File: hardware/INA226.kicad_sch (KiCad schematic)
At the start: 6 parts, among them U501 INA226

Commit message: Tracing 2
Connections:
- net VIN+ renamed VIN
- net VIN- renamed VOUT
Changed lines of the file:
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@@
 		)
 	)
-	(hierarchical_label "VIN+"
+	(hierarchical_label "VIN"
 		(shape input)
 		(at 91.44 96.52 180)
@@
 		)
 	)
-	(hierarchical_label "VIN-"
+	(hierarchical_label "VOUT"
 		(shape input)
 		(at 91.44 109.22 180)

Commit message: Tracing 3
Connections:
- net ALERT: now reaches U501.3 (~{Alert})
- no-connect marks 1 -> 0
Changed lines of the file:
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@@
 		(color 0 0 0 0)
-	)
-	(no_connect
-		(at 156.21 101.6)
 	)
 	(wire
@@
 		(effects
 			(font
+				(size 1.27 1.27)
+			)
+			(justify left)
+		)
+	)
+	(hierarchical_label "ALERT"
+		(shape input)
+		(at 156.21 101.6 0)
+		(effects
+			(font

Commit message: Fixes
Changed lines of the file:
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@@
 	)
 	(hierarchical_label "ALERT"
-		(shape input)
+		(shape output)
 		(at 156.21 101.6 0)
 		(effects

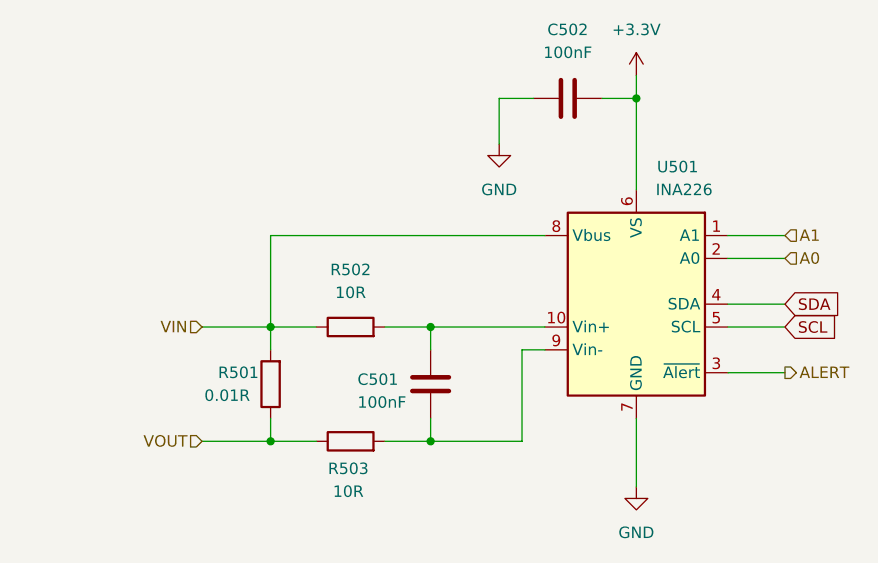
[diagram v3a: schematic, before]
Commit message: thermal relief
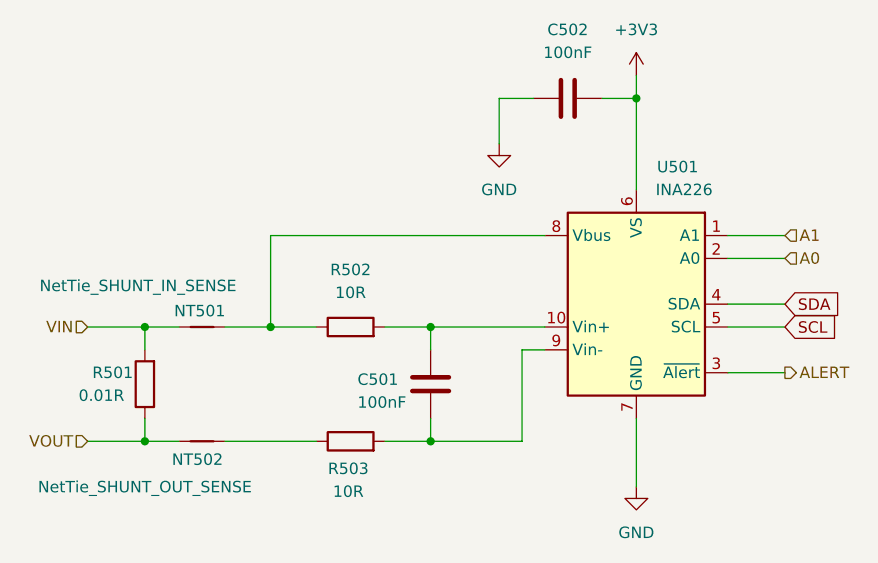
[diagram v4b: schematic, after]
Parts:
- added NT501: NetTie_SHUNT_IN_SENSE, NetTie:NetTie-2_SMD_Pad0.5mm, symbol Device:NetTie_2
- added NT502: NetTie_SHUNT_OUT_SENSE, NetTie:NetTie-2_SMD_Pad0.5mm, symbol Device:NetTie_2
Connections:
- net VIN: now also NT501.1; no longer R502.1, U501.8 (Vbus)
- net VOUT: now also NT502.1; no longer R503.1
- net +3.3V renamed +3V3
- new net: NT502.2, R503.1
- new net: NT501.2, R502.1, U501.8 (Vbus)
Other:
- moved on the sheet: R501
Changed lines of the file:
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@@
+	)
+	(junction
+		(at 85.09 109.22)
+		(diameter 0)
+		(color 0 0 0 0)
+	)
+	(junction
+		(at 85.09 96.52)
+		(diameter 0)
+		(color 0 0 0 0)
 	)
 	(junction
@@
 		(color 0 0 0 0)
 	)
-	(junction
-		(at 99.06 109.22)
-		(diameter 0)
-		(color 0 0 0 0)
-	)
-	(wire
-		(pts
-			(xy 91.44 96.52) (xy 99.06 96.52)
+	(wire
+		(pts
+			(xy 78.74 109.22) (xy 85.09 109.22)
 		)
 		(stroke
@@
 	(wire
 		(pts
-			(xy 91.44 109.22) (xy 99.06 109.22)
-		)
-		(stroke
-			(width 0)
-			(type default)
-		)
-	)
-	(wire
-		(pts
 			(xy 116.84 96.52) (xy 116.84 99.06)
 		)
@@
 	(wire
 		(pts
+			(xy 93.98 96.52) (xy 99.06 96.52)
+		)
+		(stroke
+			(width 0)
+			(type default)
+		)
+	)
+	(wire
+		(pts
 			(xy 99.06 86.36) (xy 129.54 86.36)
 		)
@@
 	(wire
 		(pts
-			(xy 104.14 109.22) (xy 99.06 109.22)
+			(xy 85.09 96.52) (xy 88.9 96.52)
+		)
+		(stroke
+			(width 0)
+			(type default)
+		)
+	)
+	(wire
+		(pts
+			(xy 93.98 109.22) (xy 104.14 109.22)
 		)
 		(stroke
@@
 	(wire
 		(pts
+			(xy 78.74 96.52) (xy 85.09 96.52)
+		)
+		(stroke
+			(width 0)
+			(type default)
+		)
+	)
+	(wire
+		(pts
 			(xy 124.46 71.12) (xy 124.46 76.2)
 		)
@@
 	(wire
 		(pts
-			(xy 99.06 96.52) (xy 99.06 99.06)
+			(xy 85.09 109.22) (xy 88.9 109.22)
 		)
 		(stroke
@@
 	(wire
 		(pts
+			(xy 85.09 109.22) (xy 85.09 106.68)
+		)
+		(stroke
+			(width 0)
+			(type default)
+		)
+	)
+	(wire
+		(pts
 			(xy 127 99.06) (xy 129.54 99.06)
 		)
@@
 	(wire
 		(pts
-			(xy 99.06 109.22) (xy 99.06 106.68)
+			(xy 85.09 96.52) (xy 85.09 99.06)
 		)
 		(stroke
@@
 	(hierarchical_label "VIN"
 		(shape input)
-		(at 91.44 96.52 180)
+		(at 78.74 96.52 180)
 		(effects
 			(font
@@
 	(hierarchical_label "VOUT"
 		(shape input)
-		(at 91.44 109.22 180)
+		(at 78.74 109.22 180)
 		(effects
 			(font
@@
 	(symbol
 		(lib_id "Device:R")
-		(at 99.06 102.87 180)
+		(at 85.09 102.87 180)
 		(unit 1)
 		(exclude_from_sim no)
@@
 		(dnp no)
 		(property "Reference" "R501"
-			(at 93.218 101.6 0)
+			(at 79.248 101.6 0)
 			(effects
 				(font
@@
 		)
 		(property "Value" "0.01R"
-			(at 91.694 104.14 0)
+			(at 77.724 104.14 0)
 			(effects
 				(font
@@
 		)
 		(property "Footprint" "Resistor_SMD:R_2512_6332Metric_Pad1.40x3.35mm_HandSolder"
-			(at 100.838 102.87 90)
+			(at 86.868 102.87 90)
 			(effects
 				(font
@@
 		)
 		(property "Datasheet" "~"
-			(at 99.06 102.87 0)
+			(at 85.09 102.87 0)
 			(effects
 				(font
@@
 		)
 		(property "Description" "Resistor"
-			(at 99.06 102.87 0)
+			(at 85.09 102.87 0)
 			(effects
 				(font
@@
 	)
 	(symbol
+		(lib_id "Device:NetTie_2")
+		(at 91.44 109.22 0)
+		(unit 1)
+		(exclude_from_sim no)
+		(in_bom no)
+		(on_board yes)
+		(dnp no)
+		(property "Reference" "NT502"
+			(at 90.932 111.252 0)
+			(effects
+				(font
+					(size 1.27 1.27)
+				)
+			)
+		)
+		(property "Value" "NetTie_SHUNT_OUT_SENSE"
+			(at 85.09 114.3 0)
+			(effects
+				(font
+					(size 1.27 1.27)
+				)
+			)
+		)
+		(property "Footprint" "NetTie:NetTie-2_SMD_Pad0.5mm"
+			(at 91.44 109.22 0)
+			(effects
+				(font
+					(size 1.27 1.27)
+				)
+				(hide yes)
+			)
+		)
+		(property "Datasheet" "~"
+			(at 91.44 109.22 0)
+			(effects
+				(font
+					(size 1.27 1.27)
+				)
+				(hide yes)
+			)
+		)
+		(property "Description" "Net tie, 2 pins"
+			(at 91.44 109.22 0)
+			(effects
+				(font
+					(size 1.27 1.27)
+				)
+				(hide yes)
+			)
+		)
+		(pin "2"
+		)
+		(pin "1"
+		)
+		(instances
+			(project ""
+				(path "/2a3ef4c2-927a-45cd-a4f2-5ee83a7e9444/4bc00da0-4814-43a9-a32d-b93b905ddfeb"
+					(reference "NT602")
+					(unit 1)
+				)
+				(path "/2a3ef4c2-927a-45cd-a4f2-5ee83a7e9444/f962763b-4c4d-46df-88bc-cd86339d95d6"
+					(reference "NT702")
+					(unit 1)
+				)
+				(path "/2a3ef4c2-927a-45cd-a4f2-5ee83a7e9444/56c5dda2-1e55-4d6c-a70d-c1acd647cefd/f8324967-96b4-4b60-9438-d68c8ddcfb61"
+					(reference "NT1202")
+					(unit 1)
+				)
+				(path "/2a3ef4c2-927a-45cd-a4f2-5ee83a7e9444/865d6fe0-7870-4134-be7f-c35221518457/f8324967-96b4-4b60-9438-d68c8ddcfb61"
+					(reference "NT502")
+					(unit 1)
+				)
+				(path "/2a3ef4c2-927a-45cd-a4f2-5ee83a7e9444/b3941ffe-e8e1-48f3-a016-360d76a87258/f8324967-96b4-4b60-9438-d68c8ddcfb61"
+					(reference "NT1002")
+					(unit 1)
+				)
+			)
+		)
+	)
+	(symbol
 		(lib_id "power:+3.3V")
 		(at 139.7 68.58 0)
@@
 			)
 		)
-		(property "Value" "+3.3V"
+		(property "Value" "+3V3"
 			(at 139.7 63.5 0)
 			(effects
@@
 					(unit 1)
 				)
+			)
+		)
+	)
+	(symbol
+		(lib_id "Device:NetTie_2")
+		(at 91.44 96.52 0)
+		(unit 1)
+		(exclude_from_sim no)
+		(in_bom no)
+		(on_board yes)
+		(dnp no)
+		(property "Reference" "NT501"
+			(at 91.186 94.742 0)
+			(effects
+				(font
+					(size 1.27 1.27)
+				)
+			)
+		)
+		(property "Value" "NetTie_SHUNT_IN_SENSE"
+			(at 84.328 91.948 0)
+			(effects
+				(font
+					(size 1.27 1.27)
+				)
+			)
+		)
+		(property "Footprint" "NetTie:NetTie-2_SMD_Pad0.5mm"
+			(at 91.44 96.52 0)
+			(effects
+				(font
+					(size 1.27 1.27)
+				)
+				(hide yes)
+			)
+		)
+		(property "Datasheet" "~"
+			(at 91.44 96.52 0)
+			(effects
+				(font
+					(size 1.27 1.27)
+				)
+				(hide yes)
+			)
+		)
+		(property "Description" "Net tie, 2 pins"
+			(at 91.44 96.52 0)
+			(effects
+				(font
+					(size 1.27 1.27)
+				)
+				(hide yes)
+			)
+		)
+		(pin "1"
+		)
+		(pin "2"
+		)
+		(instances
+			(project ""
+				(path "/2a3ef4c2-927a-45cd-a4f2-5ee83a7e9444/4bc00da0-4814-43a9-a32d-b93b905ddfeb"
+					(reference "NT601")
+					(unit 1)
+				)
+				(path "/2a3ef4c2-927a-45cd-a4f2-5ee83a7e9444/f962763b-4c4d-46df-88bc-cd86339d95d6"
+					(reference "NT701")
+					(unit 1)
+				)
+				(path "/2a3ef4c2-927a-45cd-a4f2-5ee83a7e9444/56c5dda2-1e55-4d6c-a70d-c1acd647cefd/f8324967-96b4-4b60-9438-d68c8ddcfb61"
+					(reference "NT1201")
+					(unit 1)
+				)
+				(path "/2a3ef4c2-927a-45cd-a4f2-5ee83a7e9444/865d6fe0-7870-4134-be7f-c35221518457/f8324967-96b4-4b60-9438-d68c8ddcfb61"
+					(reference "NT501")
+					(unit 1)
+				)
+				(path "/2a3ef4c2-927a-45cd-a4f2-5ee83a7e9444/b3941ffe-e8e1-48f3-a016-360d76a87258/f8324967-96b4-4b60-9438-d68c8ddcfb61"
+					(reference "NT1001")
+					(unit 1)
+				)

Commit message: tracing
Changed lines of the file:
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@@
 		)
 		(property "Value" "NetTie_SHUNT_OUT_SENSE"
-			(at 85.09 114.3 0)
+			(at 89.408 114.046 0)
 			(effects
 				(font

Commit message: reanotate
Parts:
- renumbered C501 to C301, C502 to C302, NT501 to NT301, NT502 to NT302, R501 to R301, R502 to R302, R503 to R303, U501 to U301

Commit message: hand soldering footprints and led
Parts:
- C301, C302: footprint Capacitor_SMD:C_0603_1608Metric -> Capacitor_SMD:C_0603_1608Metric_Pad1.08x0.95mm_HandSolder
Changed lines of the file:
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@@
 			)
 		)
-		(property "Footprint" "Capacitor_SMD:C_0603_1608Metric"
+		(property "Footprint" "Capacitor_SMD:C_0603_1608Metric_Pad1.08x0.95mm_HandSolder"
 			(at 128.27 72.0852 0)
 			(effects
@@
 			)
 		)
-		(property "Footprint" "Capacitor_SMD:C_0603_1608Metric"
+		(property "Footprint" "Capacitor_SMD:C_0603_1608Metric_Pad1.08x0.95mm_HandSolder"
 			(at 117.8052 106.68 0)
 			(effects
